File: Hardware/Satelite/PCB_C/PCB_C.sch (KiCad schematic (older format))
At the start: 36 parts, among them IC1 MCP1501T-33E_CHY, IC3 BQ24392RSER, J1 Conn_01x06, J3 Conector_PCB_B-C, J4 Conector_Expansion_CanSat, J5 USB_B_Micro, J6 Conn_02x03_Counter_Clockwise, M1 Spacer, M2 Spacer, M3 Spacer, U1 NTB0104BQ,115, U2 TCA9802DGKR, U3 ESP32-WROOM-32, U4 NTB0104BQ,115, U7 PIC16LF18325-ISL, Y1 LFXTAL016178

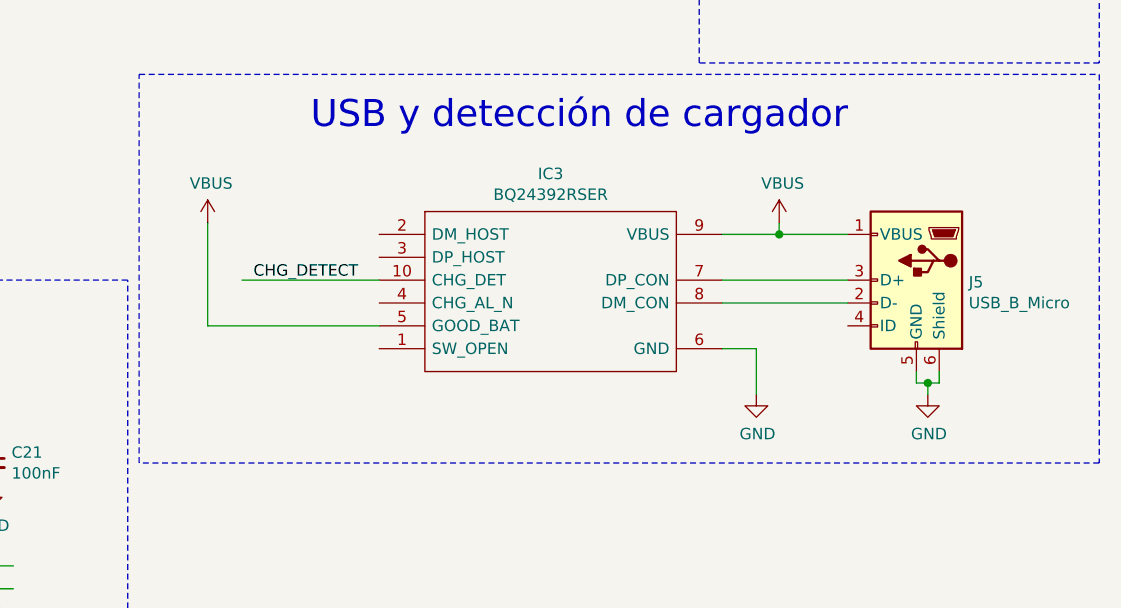
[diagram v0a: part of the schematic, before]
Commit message: Uso de 3.3V internos para todos los sensores en PCB_C y agregado de divisor resistivo para la señal de 5V proveniente del BQ24392.
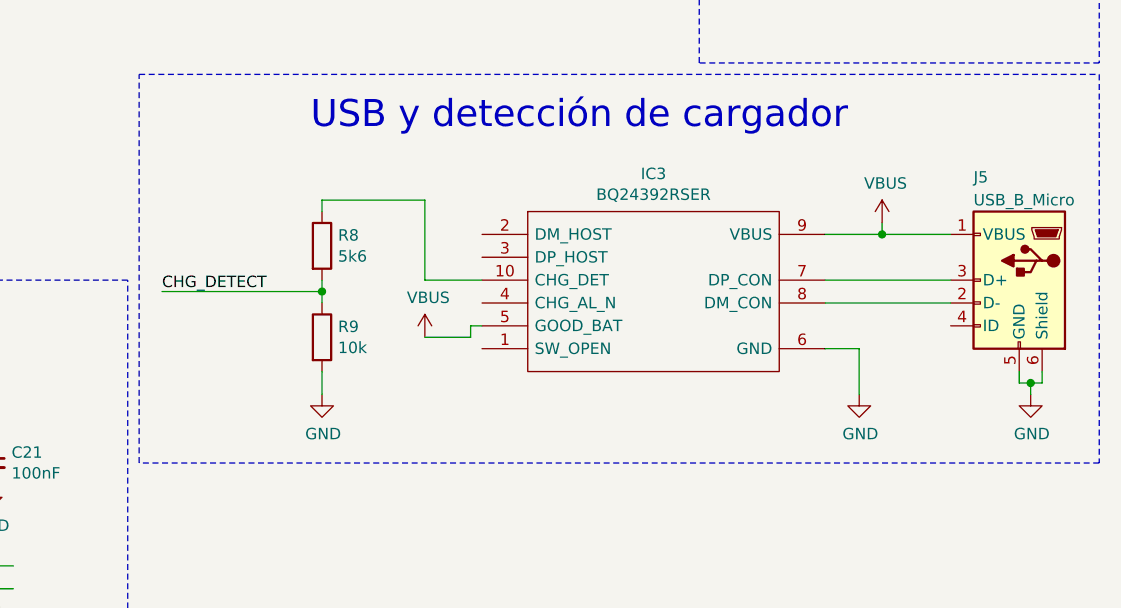
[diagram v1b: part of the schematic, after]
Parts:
- added R8: 5k6, Resistor_SMD:R_0603_1608Metric_Pad1.05x0.95mm_HandSolder, symbol Device:R
- added R9: 10k, Resistor_SMD:R_0603_1608Metric_Pad1.05x0.95mm_HandSolder, symbol Device:R
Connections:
- wire segments 277 -> 285
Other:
- moved on the sheet: IC3, J5
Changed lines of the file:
@@
 L Connector:USB_B_Micro J5
 U 1 1 5BBBF74C
-P 15200 9000
-F 0 "J5" H 14971 8991 50  0000 R CNN
-F 1 "USB_B_Micro" H 14971 8900 50  0000 R CNN
-F 2 "Connector_USB:USB_Micro-B_Molex-105017-0001" H 15350 8950 50  0001 C CNN
-F 3 "https://www.molex.com/webdocs/datasheets/pdf/en-us/1050170001_IO_CONNECTORS.pdf" H 15350 8950 50  0001 C CNN
-F 4 "105017-0001" H 15200 9000 50  0001 C CNN "Manufacturer Part Number"
-	1    15200 9000
+P 15650 9000
+F 0 "J5" H 15850 9450 50  0000 R CNN
+F 1 "USB_B_Micro" H 15850 9350 50  0000 R CNN
+F 2 "Connector_USB:USB_Micro-B_Molex-105017-0001" H 15800 8950 50  0001 C CNN
+F 3 "https://www.molex.com/webdocs/datasheets/pdf/en-us/1050170001_IO_CONNECTORS.pdf" H 15800 8950 50  0001 C CNN
+F 4 "105017-0001" H 15650 9000 50  0001 C CNN "Manufacturer Part Number"
+	1    15650 9000
 	-1   0    0    -1
 $EndComp
@@
 L power:VBUS #PWR059
 U 1 1 5BBBFAE6
-P 14600 8750
-F 0 "#PWR059" H 14600 8600 50  0001 C CNN
-F 1 "VBUS" H 14615 8923 50  0000 C CNN
-F 2 "" H 14600 8750 50  0001 C CNN
-F 3 "" H 14600 8750 50  0001 C CNN
-	1    14600 8750
+P 15050 8750
+F 0 "#PWR059" H 15050 8600 50  0001 C CNN
+F 1 "VBUS" H 15065 8923 50  0000 C CNN
+F 2 "" H 15050 8750 50  0001 C CNN
+F 3 "" H 15050 8750 50  0001 C CNN
+	1    15050 8750
 	1    0    0    -1
 $EndComp
@@
 L power:GND #PWR061
 U 1 1 5BBC2A6C
-P 15250 9500
-F 0 "#PWR061" H 15250 9250 50  0001 C CNN
-F 1 "GND" H 15255 9327 50  0000 C CNN
-F 2 "" H 15250 9500 50  0001 C CNN
-F 3 "" H 15250 9500 50  0001 C CNN
-	1    15250 9500
-	1    0    0    -1
-$EndComp
-Wire Wire Line
-	14900 9100 14350 9100
-Wire Wire Line
-	14350 9000 14900 9000
-Wire Wire Line
-	15200 9400 15200 9450
-Wire Wire Line
-	15200 9450 15250 9450
-Wire Wire Line
-	15300 9400 15300 9450
-Wire Wire Line
-	15300 9450 15250 9450
+P 15700 9500
+F 0 "#PWR061" H 15700 9250 50  0001 C CNN
+F 1 "GND" H 15705 9327 50  0000 C CNN
+F 2 "" H 15700 9500 50  0001 C CNN
+F 3 "" H 15700 9500 50  0001 C CNN
+	1    15700 9500
+	1    0    0    -1
+$EndComp
+Wire Wire Line
+	15350 9100 14800 9100
+Wire Wire Line
+	14800 9000 15350 9000
+Wire Wire Line
+	15650 9400 15650 9450
+Wire Wire Line
+	15650 9450 15700 9450
+Wire Wire Line
+	15750 9400 15750 9450
+Wire Wire Line
+	15750 9450 15700 9450
 $Comp
 L SamacSys_Parts:BQ24392RSER IC3
 U 1 1 5BBE8A84
-P 12850 8800
-F 0 "IC3" H 13600 9065 50  0000 C CNN
-F 1 "BQ24392RSER" H 13600 8974 50  0000 C CNN
-F 2 "SamacSys_Parts:RSE(R-PUQFN-N10)" H 14200 8900 50  0001 L CNN
-F 3 "http://www.ti.com/lit/gpn/bq24392" H 14200 8800 50  0001 L CNN
-F 4 "SPST USB 2.0 High-Speed Switch With Battery Charging Detection" H 14200 8700 50  0001 L CNN "Description"
-F 5 "Texas Instruments" H 14200 8500 50  0001 L CNN "Manufacturer_Name"
-F 6 "BQ24392RSER" H 14200 8400 50  0001 L CNN "Manufacturer Part Number"
-F 7 "8279327P" H 14200 8300 50  0001 L CNN "RS Part Number"
-F 8 "http://uk.rs-online.com/web/p/products/8279327P" H 14200 8200 50  0001 L CNN "RS Price/Stock"
-F 9 "BQ24392RSER" H 14200 8100 50  0001 L CNN "Arrow Part Number"
-F 10 "https://www.arrow.com/en/products/bq24392rser/texas-instruments" H 14200 8000 50  0001 L CNN "Arrow Price/Stock"
-	1    12850 8800
-	1    0    0    -1
-$EndComp
-Wire Wire Line
-	14350 8800 14600 8800
-Wire Wire Line
-	14600 8750 14600 8800
-Connection ~ 14600 8800
-Wire Wire Line
-	14600 8800 14900 8800
+P 13300 8800
+F 0 "IC3" H 14050 9065 50  0000 C CNN
+F 1 "BQ24392RSER" H 14050 8974 50  0000 C CNN
+F 2 "SamacSys_Parts:RSE(R-PUQFN-N10)" H 14650 8900 50  0001 L CNN
+F 3 "http://www.ti.com/lit/gpn/bq24392" H 14650 8800 50  0001 L CNN
+F 4 "SPST USB 2.0 High-Speed Switch With Battery Charging Detection" H 14650 8700 50  0001 L CNN "Description"
+F 5 "Texas Instruments" H 14650 8500 50  0001 L CNN "Manufacturer_Name"
+F 6 "BQ24392RSER" H 14650 8400 50  0001 L CNN "Manufacturer Part Number"
+F 7 "8279327P" H 14650 8300 50  0001 L CNN "RS Part Number"
+F 8 "http://uk.rs-online.com/web/p/products/8279327P" H 14650 8200 50  0001 L CNN "RS Price/Stock"
+F 9 "BQ24392RSER" H 14650 8100 50  0001 L CNN "Arrow Part Number"
+F 10 "https://www.arrow.com/en/products/bq24392rser/texas-instruments" H 14650 8000 50  0001 L CNN "Arrow Price/Stock"
+	1    13300 8800
+	1    0    0    -1
+$EndComp
+Wire Wire Line
+	14800 8800 15050 8800
+Wire Wire Line
+	15050 8750 15050 8800
+Connection ~ 15050 8800
+Wire Wire Line
+	15050 8800 15350 8800
 $Comp
 L power:GND #PWR058
 U 1 1 5BBEBEBA
-P 14500 9500
-F 0 "#PWR058" H 14500 9250 50  0001 C CNN
-F 1 "GND" H 14505 9327 50  0000 C CNN
-F 2 "" H 14500 9500 50  0001 C CNN
-F 3 "" H 14500 9500 50  0001 C CNN
-	1    14500 9500
-	1    0    0    -1
-$EndComp
-Wire Wire Line
-	14350 9300 14500 9300
-Wire Wire Line
-	14500 9300 14500 9500
-Wire Wire Line
-	12850 9000 12250 9000
-Text Label 12300 9000 0    50   ~ 0
+P 14950 9500
+F 0 "#PWR058" H 14950 9250 50  0001 C CNN
+F 1 "GND" H 14955 9327 50  0000 C CNN
+F 2 "" H 14950 9500 50  0001 C CNN
+F 3 "" H 14950 9500 50  0001 C CNN
+	1    14950 9500
+	1    0    0    -1
+$EndComp
+Wire Wire Line
+	14800 9300 14950 9300
+Wire Wire Line
+	14950 9300 14950 9500
+Text Label 11900 9050 0    50   ~ 0
 CHG_DETECT
 $Comp
 L power:VBUS #PWR045
 U 1 1 5BC0A264
-P 12100 8750
-F 0 "#PWR045" H 12100 8600 50  0001 C CNN
-F 1 "VBUS" H 12115 8923 50  0000 C CNN
-F 2 "" H 12100 8750 50  0001 C CNN
-F 3 "" H 12100 8750 50  0001 C CNN
-	1    12100 8750
-	1    0    0    -1
-$EndComp
-Wire Wire Line
-	12100 8750 12100 9200
-Wire Wire Line
-	12100 9200 12850 9200
+P 13050 9250
+F 0 "#PWR045" H 13050 9100 50  0001 C CNN
+F 1 "VBUS" H 13065 9423 50  0000 C CNN
+F 2 "" H 13050 9250 50  0001 C CNN
+F 3 "" H 13050 9250 50  0001 C CNN
+	1    13050 9250
+	1    0    0    -1
+$EndComp
 Wire Notes Line
 	11800 8100 16000 8100
@@
 Wire Wire Line
 	15600 1500 15000 1500
-Connection ~ 15250 9450
-Wire Wire Line
-	15250 9450 15250 9500
+Connection ~ 15700 9450
+Wire Wire Line
+	15700 9450 15700 9500
 $Comp
 L power:+BATT #PWR053
@@
 	1150 5850 1150 5750
 $Comp
-L power:+BATT #PWR01
-U 1 1 5BC3E6F0
-P 1150 5750
-F 0 "#PWR01" H 1150 5600 50  0001 C CNN
-F 1 "+BATT" H 1165 5923 50  0000 C CNN
-F 2 "" H 1150 5750 50  0001 C CNN
-F 3 "" H 1150 5750 50  0001 C CNN
-	1    1150 5750
-	-1   0    0    -1
-$EndComp
-$Comp
 L SamacSys_Parts:MCP1501T-33E_CHY IC1
 U 1 1 5BC3E089
@@
 Wire Wire Line
 	15100 4650 15550 4650
+$Comp
+L Device:R R8
+U 1 1 5C2BF325
+P 12600 8850
+F 0 "R8" H 12670 8896 50  0000 L CNN
+F 1 "5k6" H 12670 8804 50  0000 L CNN
+F 2 "Resistor_SMD:R_0603_1608Metric_Pad1.05x0.95mm_HandSolder" V 12530 8850 50  0001 C CNN
+F 3 "~" H 12600 8850 50  0001 C CNN
+F 4 "RC0603FR-075K6L" H 12600 8850 50  0001 C CNN "Manufacturer Part Number"
+	1    12600 8850
+	1    0    0    -1
+$EndComp
+Wire Wire Line
+	13050 9250 13250 9250
+Wire Wire Line
+	13250 9250 13250 9200
+Wire Wire Line
+	13250 9200 13300 9200
+$Comp
+L Device:R R9
+U 1 1 5C3B0D3B
+P 12600 9250
+F 0 "R9" H 12670 9296 50  0000 L CNN
+F 1 "10k" H 12670 9204 50  0000 L CNN
+F 2 "Resistor_SMD:R_0603_1608Metric_Pad1.05x0.95mm_HandSolder" V 12530 9250 50  0001 C CNN
+F 3 "~" H 12600 9250 50  0001 C CNN
+F 4 "RC0603JR-0710KL" H 12600 9250 50  0001 C CNN "Manufacturer Part Number"
+	1    12600 9250
+	1    0    0    -1
+$EndComp
+Wire Wire Line
+	13300 9000 13050 9000
+Wire Wire Line
+	13050 9000 13050 8650
+Wire Wire Line
+	13050 8650 12600 8650
+$Comp
+L power:GND #PWR011
+U 1 1 5C412A14
+P 12600 9500
+F 0 "#PWR011" H 12600 9250 50  0001 C CNN
+F 1 "GND" H 12605 9327 50  0000 C CNN
+F 2 "" H 12600 9500 50  0001 C CNN
+F 3 "" H 12600 9500 50  0001 C CNN
+	1    12600 9500
+	1    0    0    -1
+$EndComp
+Wire Wire Line
+	12600 9400 12600 9500
+Wire Wire Line
+	12600 9000 12600 9050
+Wire Wire Line
+	12600 8650 12600 8700
+Wire Wire Line
+	12600 9100 12600 9050
+Connection ~ 12600 9050
+$Comp
+L power:+BATT #PWR01
+U 1 1 5BC3E6F0
+P 1150 5750
+F 0 "#PWR01" H 1150 5600 50  0001 C CNN
+F 1 "+BATT" H 1165 5923 50  0000 C CNN
+F 2 "" H 1150 5750 50  0001 C CNN
+F 3 "" H 1150 5750 50  0001 C CNN
+	1    1150 5750
+	-1   0    0    -1
+$EndComp
+Wire Wire Line
+	11900 9050 12600 9050
 $EndSCHEMATC

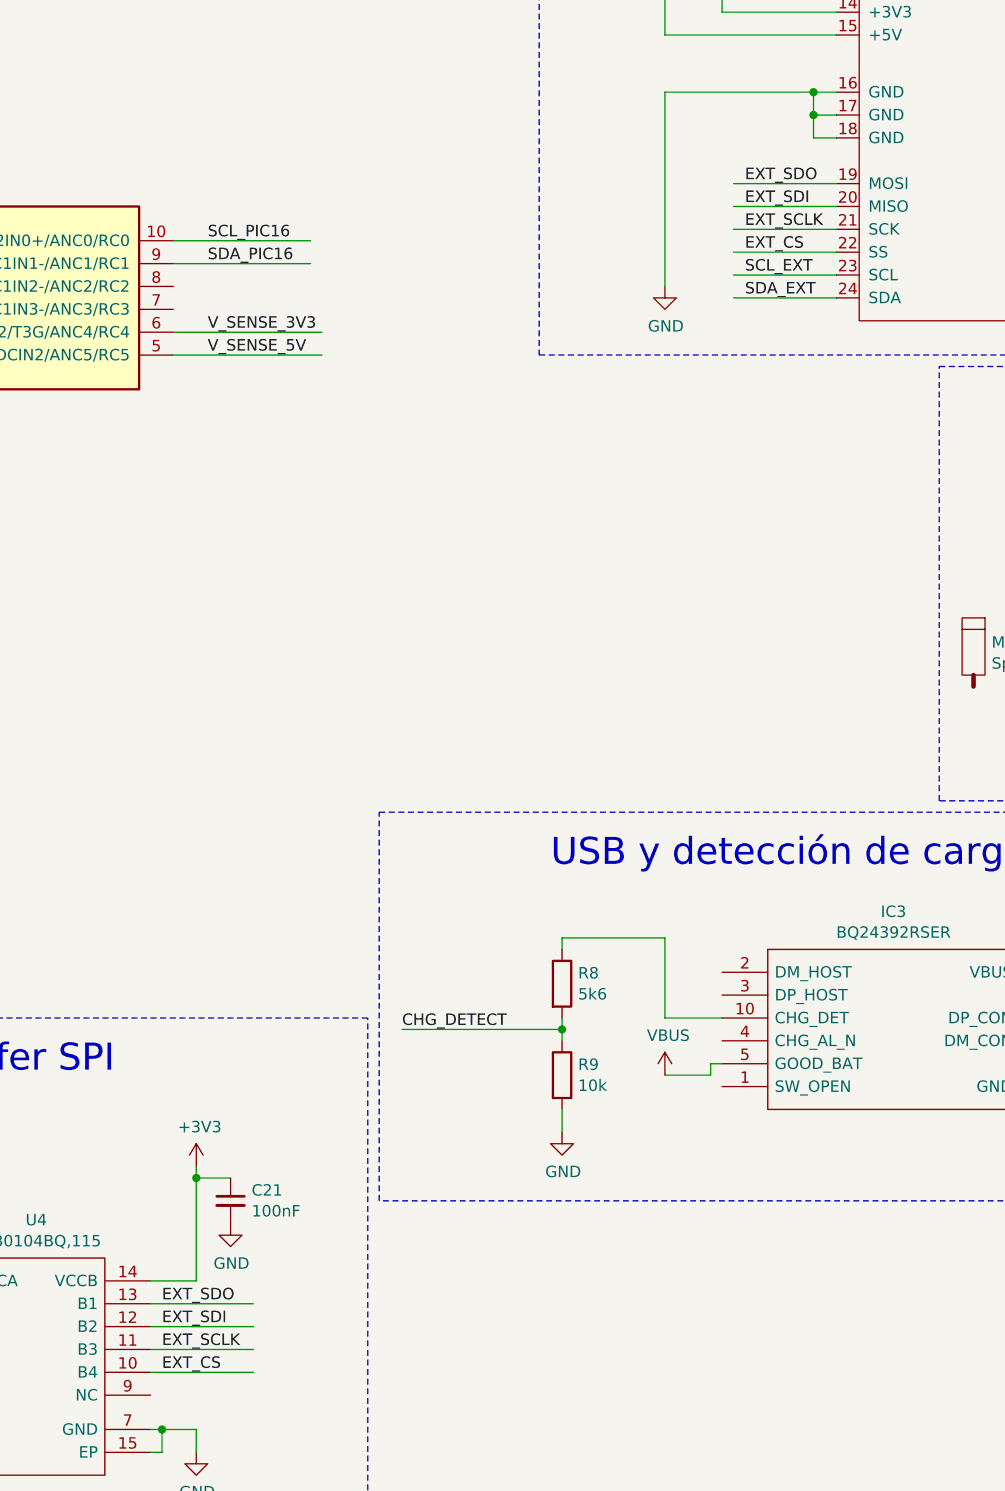
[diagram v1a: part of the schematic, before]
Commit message: Corregido MISO y MOSI al revés
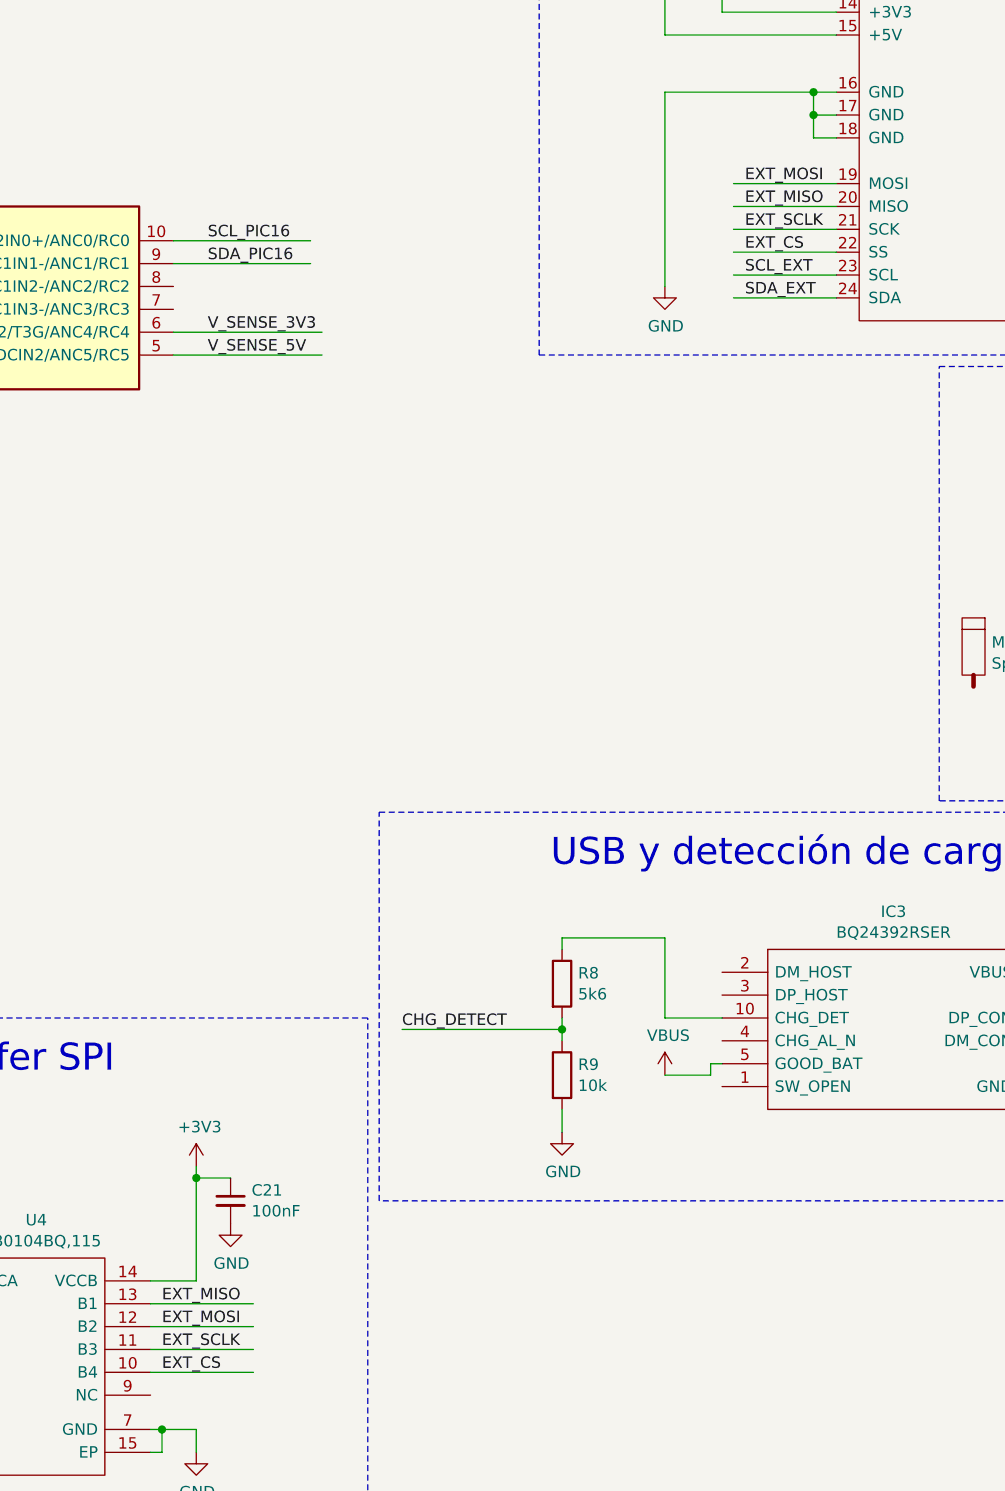
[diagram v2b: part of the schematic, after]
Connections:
- net labels added: EXT_MISO, EXT_MOSI
- net labels removed: EXT_SDI, EXT_SDO
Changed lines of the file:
@@
 	11250 10550 10800 10550
 Text Label 10850 10250 0    50   ~ 0
-EXT_SDO
+EXT_MISO
 Text Label 10850 10350 0    50   ~ 0
-EXT_SDI
+EXT_MOSI
 Text Label 10850 10450 0    50   ~ 0
 EXT_SCLK
@@
 	13350 5850 13800 5850
 Text Label 13400 5350 0    50   ~ 0
-EXT_SDO
+EXT_MOSI
 Text Label 13400 5450 0    50   ~ 0
-EXT_SDI
+EXT_MISO
 Text Label 13400 5550 0    50   ~ 0
 EXT_SCLK

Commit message: Modelos 3D faltantes en PCB_C
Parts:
- J4: Manufacturer Part Number (none) -> SSQ-106-03-T-S; Quantity (none) -> 4
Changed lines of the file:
@@
 F 2 "" H 14450 5500 50  0001 C CNN
 F 3 "" H 14450 5500 50  0001 C CNN
+F 4 "SSQ-106-03-T-S" H 14450 5000 50  0001 C CNN "Manufacturer Part Number"
+F 5 "4" H 14450 5000 50  0001 C CNN "Quantity"
 	1    14450 5000
 	1    0    0    -1

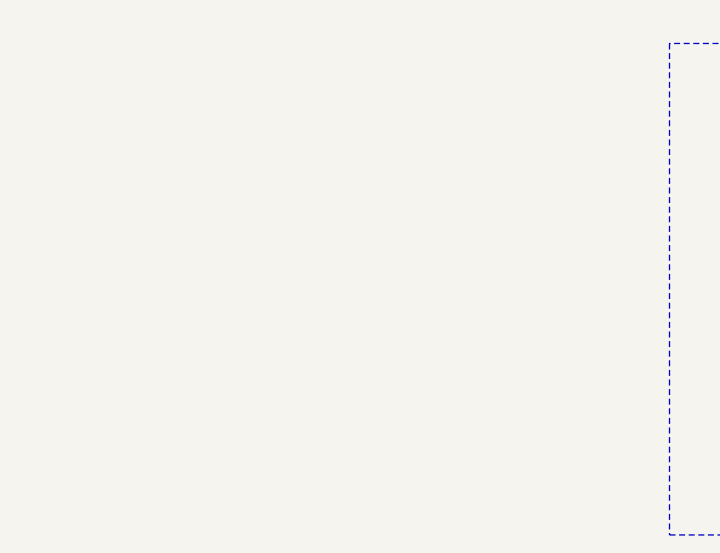
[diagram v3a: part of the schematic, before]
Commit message: Logo open hardware en esquemáticos
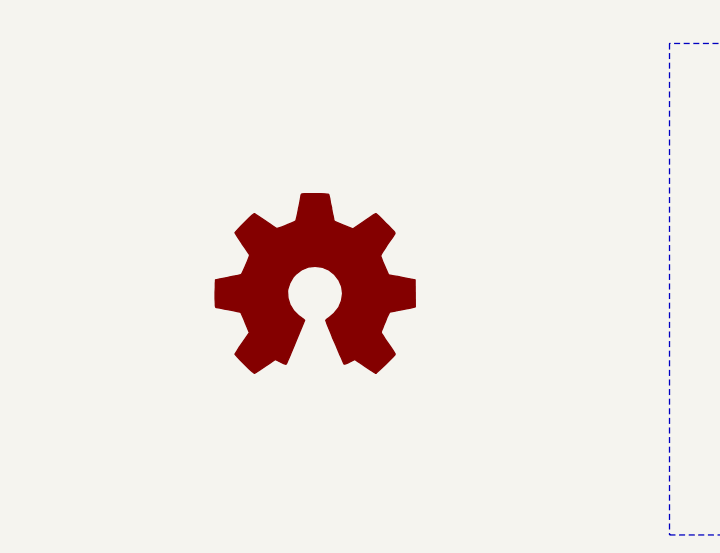
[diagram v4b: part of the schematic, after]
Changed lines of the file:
@@
 Wire Wire Line
 	11900 9050 12600 9050
+$Comp
+L Graphic:Logo_Open_Hardware_Large #LOGO?
+U 1 1 5C32959E
+P 1850 10100
+F 0 "#LOGO?" H 1850 10600 50  0001 C CNN
+F 1 "Logo_Open_Hardware_Large" H 1850 9700 50  0001 C CNN
+F 2 "" H 1850 10100 50  0001 C CNN
+F 3 "~" H 1850 10100 50  0001 C CNN
+	1    1850 10100
+	1    0    0    -1
+$EndComp
 $EndSCHEMATC

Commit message: Actualización de BOM
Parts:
- U3: symbol RF_Module:ESP32-WROOM-32 -> PCB_C-rescue:ESP32-WROOM-32-RF_Module; Manufacturer Part Number (none) -> ESP32-WROOM-32
- U7: Manufacturer Part Number (none) -> PIC16LF18325-I/SL
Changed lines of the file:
@@
 	8150 7350 7750 7350
 $Comp
-L RF_Module:ESP32-WROOM-32 U3
+L PCB_C-rescue:ESP32-WROOM-32-RF_Module U3
 U 1 1 5D74DFF0
 P 6650 2850
@@
 F 2 "RF_Module:ESP32-WROOM-32" H 6650 1350 50  0001 C CNN
 F 3 "https://www.espressif.com/sites/default/files/documentation/esp32-wroom-32_datasheet_en.pdf" H 6350 2900 50  0001 C CNN
+F 4 "ESP32-WROOM-32" H 6650 2850 50  0001 C CNN "Manufacturer Part Number"
 	1    6650 2850
 	1    0    0    -1
@@
 F 2 "Package_SO:SOIC-14_3.9x8.7mm_P1.27mm" H 8400 5300 50  0001 C CNN
 F 3 "http://ww1.microchip.com/downloads/en/devicedoc/40001795b.pdf" H 8400 5200 50  0001 C CNN
+F 4 "PIC16LF18325-I/SL" H 8400 5900 50  0001 C CNN "Manufacturer Part Number"
 	1    8400 5900
 	1    0    0    -1
@@
 	11900 9050 12600 9050
 $Comp
-L Graphic:Logo_Open_Hardware_Large #LOGO?
+L Graphic:Logo_Open_Hardware_Large #LOGO1
 U 1 1 5C32959E
 P 1850 10100
-F 0 "#LOGO?" H 1850 10600 50  0001 C CNN
+F 0 "#LOGO1" H 1850 10600 50  0001 C CNN
 F 1 "Logo_Open_Hardware_Large" H 1850 9700 50  0001 C CNN
 F 2 "" H 1850 10100 50  0001 C CNN
